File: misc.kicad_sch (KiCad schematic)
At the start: 9 parts, among them J1 BUZZER, J2 BURNER, J3 BATT, Q1 PSMN7R0, Q2 PSMN7R0

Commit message: First version for PCB
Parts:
- added J4: BAKCBONE, Connector_PinSocket_2.54mm:PinSocket_2x10_P2.54mm_Horizontal, symbol Connector_Generic:Conn_02x10_Odd_Even
- R10, R9: footprint Resistor_SMD:R_0603_1608Metric -> Resistor_SMD:R_0402_1005Metric
- R11: value 10k -> 55k
- R12: value 5k -> 55k
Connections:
- net BURNER: now also J4.13 (Pin_13), J4.14 (Pin_14)
- net BUZZER: now also J4.15 (Pin_15), J4.16 (Pin_16)
- net GND: now also J4.1 (Pin_1), J4.19 (Pin_19), J4.2 (Pin_2), J4.20 (Pin_20)
- net VOLT_SENSE: now also J4.7 (Pin_7), J4.8 (Pin_8)
- new net +3.3V: J4.17 (Pin_17), J4.18 (Pin_18)
- new net +4V: J4.3 (Pin_3), J4.4 (Pin_4)
- new net CURR_3V3: J4.11 (Pin_11), J4.12 (Pin_12)
- new net CURR_4V: J4.10 (Pin_10), J4.9 (Pin_9)
- no-connect marks 0 -> 2
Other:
- note added: "TO BACKBONE"

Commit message: Added debug things
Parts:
- added J5: DEB, Connector_PinSocket_2.54mm:PinSocket_1x06_P2.54mm_Vertical, symbol Connector_Generic:Conn_01x06
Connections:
- net +3.3V: now also J5.3 (Pin_3)
- net +4V: now also J5.2 (Pin_2)
- net BURNER: now also J5.5 (Pin_5)
- net BUZZER: now also J5.4 (Pin_4)
- net GND: now also J5.1 (Pin_1)
- net VDD: now also J5.6 (Pin_6)
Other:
- note added: "DEBUG"
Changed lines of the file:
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@@
+    (stroke (width 0) (type default) (color 0 0 0 0))
+  )
+  (wire (pts (xy 176.53 121.92) (xy 177.8 121.92))
+    (stroke (width 0) (type default) (color 0 0 0 0))
+  )
+  (polyline (pts (xy 152.4 88.9) (xy 152.4 139.7))
+    (stroke (width 0) (type default) (color 0 0 0 0))
+  )
+  (wire (pts (xy 176.53 114.3) (xy 177.8 114.3))
     (stroke (width 0) (type default) (color 0 0 0 0))
   )
@@
     (stroke (width 0) (type default) (color 0 0 0 0))
   )
+  (polyline (pts (xy 203.2 139.7) (xy 203.2 88.9))
+    (stroke (width 0) (type default) (color 0 0 0 0))
+  )
   (polyline (pts (xy 76.2 76.2) (xy 25.4 76.2))
     (stroke (width 0) (type default) (color 0 0 0 0))
@@
     (stroke (width 0) (type default) (color 0 0 0 0))
   )
+  (polyline (pts (xy 152.4 88.9) (xy 203.2 88.9))
+    (stroke (width 0) (type default) (color 0 0 0 0))
+  )
+  (wire (pts (xy 176.53 119.38) (xy 177.8 119.38))
+    (stroke (width 0) (type default) (color 0 0 0 0))
+  )
   (wire (pts (xy 55.88 44.45) (xy 54.61 44.45))
     (stroke (width 0) (type default) (color 0 0 0 0))
@@
     (stroke (width 0) (type default) (color 0 0 0 0))
   )
+  (wire (pts (xy 177.8 111.76) (xy 177.8 110.49))
+    (stroke (width 0) (type default) (color 0 0 0 0))
+  )
   (wire (pts (xy 115.57 121.92) (xy 115.57 123.19))
     (stroke (width 0) (type default) (color 0 0 0 0))
@@
     (stroke (width 0) (type default) (color 0 0 0 0))
   )
+  (wire (pts (xy 177.8 124.46) (xy 177.8 125.73))
+    (stroke (width 0) (type default) (color 0 0 0 0))
+  )
   (wire (pts (xy 151.13 184.15) (xy 151.13 185.42))
     (stroke (width 0) (type default) (color 0 0 0 0))
   )
+  (wire (pts (xy 176.53 111.76) (xy 177.8 111.76))
+    (stroke (width 0) (type default) (color 0 0 0 0))
+  )
+  (wire (pts (xy 176.53 116.84) (xy 177.8 116.84))
+    (stroke (width 0) (type default) (color 0 0 0 0))
+  )
   (wire (pts (xy 184.15 63.5) (xy 185.42 63.5))
     (stroke (width 0) (type default) (color 0 0 0 0))
@@
     (stroke (width 0) (type default) (color 0 0 0 0))
   )
+  (polyline (pts (xy 152.4 139.7) (xy 203.2 139.7))
+    (stroke (width 0) (type default) (color 0 0 0 0))
+  )
   (wire (pts (xy 151.13 176.53) (xy 151.13 177.8))
     (stroke (width 0) (type default) (color 0 0 0 0))
@@
   )
   (wire (pts (xy 55.88 124.46) (xy 55.88 127))
+    (stroke (width 0) (type default) (color 0 0 0 0))
+  )
+  (wire (pts (xy 176.53 124.46) (xy 177.8 124.46))
     (stroke (width 0) (type default) (color 0 0 0 0))
   )
@@
     (effects (font (size 2.54 2.54)) (justify left bottom))
   )
+  (text "DEBUG" (at 157.48 97.79 0)
+    (effects (font (size 2.54 2.54)) (justify left bottom))
+  )
   (text "WIRE BURNER" (at 30.48 97.79 0)
     (effects (font (size 2.54 2.54)) (justify left bottom))
@@
     )
   )
+  (global_label "3V3" (shape input) (at 177.8 119.38 0) (fields_autoplaced)
+    (effects (font (size 1.27 1.27)) (justify left))
+    (property "Intersheet References" "${INTERSHEET_REFS}" (id 0) (at 183.7207 119.4594 0)
+      (effects (font (size 1.27 1.27)) (justify left) hide)
+    )
+  )
   (global_label "BUZZER" (shape input) (at 39.37 55.88 180) (fields_autoplaced)
     (effects (font (size 1.27 1.27)) (justify right))
@@
     )
   )
+  (global_label "BUZZER" (shape input) (at 177.8 116.84 0) (fields_autoplaced)
+    (effects (font (size 1.27 1.27)) (justify left))
+    (property "Intersheet References" "${INTERSHEET_REFS}" (id 0) (at 187.6517 116.9194 0)
+      (effects (font (size 1.27 1.27)) (justify left) hide)
+    )
+  )
   (global_label "VOLT_SENSE" (shape input) (at 185.42 50.8 0) (fields_autoplaced)
     (effects (font (size 1.27 1.27)) (justify left))
@@
     )
   )
+  (global_label "BURNER" (shape input) (at 177.8 114.3 0) (fields_autoplaced)
+    (effects (font (size 1.27 1.27)) (justify left))
+    (property "Intersheet References" "${INTERSHEET_REFS}" (id 0) (at 187.8331 114.3794 0)
+      (effects (font (size 1.27 1.27)) (justify left) hide)
+    )
+  )
   (global_label "BUZZER" (shape input) (at 185.42 60.96 0) (fields_autoplaced)
     (effects (font (size 1.27 1.27)) (justify left))
@@
     (effects (font (size 1.27 1.27)) (justify left))
     (property "Intersheet References" "${INTERSHEET_REFS}" (id 0) (at 196.2393 53.2606 0)
+      (effects (font (size 1.27 1.27)) (justify left) hide)
+    )
+  )
+  (global_label "4V" (shape input) (at 177.8 121.92 0) (fields_autoplaced)
+    (effects (font (size 1.27 1.27)) (justify left))
+    (property "Intersheet References" "${INTERSHEET_REFS}" (id 0) (at 182.5112 121.9994 0)
       (effects (font (size 1.27 1.27)) (justify left) hide)
     )
@@
     (pin "1")
   )
+  (symbol (lib_id "power:VDD") (at 177.8 110.49 0) (unit 1)
+    (in_bom yes) (on_board yes) (fields_autoplaced)
+    (property "Reference" "#PWR0134" (id 0) (at 177.8 114.3 0)
+      (effects (font (size 1.27 1.27)) hide)
+    )
+    (property "Value" "VDD" (id 1) (at 177.8 105.41 0))
+    (property "Footprint" "" (id 2) (at 177.8 110.49 0)
+      (effects (font (size 1.27 1.27)) hide)
+    )
+    (property "Datasheet" "" (id 3) (at 177.8 110.49 0)
+      (effects (font (size 1.27 1.27)) hide)
+    )
+    (pin "1")
+  )
   (symbol (lib_id "power:+4V") (at 151.13 176.53 0) (unit 1)
     (in_bom yes) (on_board yes) (fields_autoplaced)
-    (property "Reference" "#PWR?" (id 0) (at 151.13 180.34 0)
+    (property "Reference" "#PWR0132" (id 0) (at 151.13 180.34 0)
       (effects (font (size 1.27 1.27)) hide)
     )
@@
     (pin "1")
   )
+  (symbol (lib_id "Connector_Generic:Conn_01x06") (at 171.45 119.38 180) (unit 1)
+    (in_bom yes) (on_board yes) (fields_autoplaced)
+    (property "Reference" "J5" (id 0) (at 171.45 105.41 0))
+    (property "Value" "DEB" (id 1) (at 171.45 107.95 0))
+    (property "Footprint" "Connector_PinSocket_2.54mm:PinSocket_1x06_P2.54mm_Vertical" (id 2) (at 171.45 119.38 0)
+      (effects (font (size 1.27 1.27)) hide)
+    )
+    (property "Datasheet" "~" (id 3) (at 171.45 119.38 0)
+      (effects (font (size 1.27 1.27)) hide)
+    )
+    (pin "1")
+    (pin "2")
+    (pin "3")
+    (pin "4")
+    (pin "5")
+    (pin "6")
+  )
   (symbol (lib_id "power:GND") (at 109.22 50.8 0) (unit 1)
     (in_bom yes) (on_board yes) (fields_autoplaced)
@@
     (pin "2")
   )
+  (symbol (lib_id "power:GND") (at 177.8 125.73 0) (unit 1)
+    (in_bom yes) (on_board yes) (fields_autoplaced)
+    (property "Reference" "#PWR0135" (id 0) (at 177.8 132.08 0)
+      (effects (font (size 1.27 1.27)) hide)
+    )
+    (property "Value" "GND" (id 1) (at 177.8 130.81 0))
+    (property "Footprint" "" (id 2) (at 177.8 125.73 0)
+      (effects (font (size 1.27 1.27)) hide)
+    )
+    (property "Datasheet" "" (id 3) (at 177.8 125.73 0)
+      (effects (font (size 1.27 1.27)) hide)
+    )
+    (pin "1")
+  )
   (symbol (lib_id "power:VDD") (at 55.88 40.64 0) (unit 1)
     (in_bom yes) (on_board yes) (fields_autoplaced)
@@
   (symbol (lib_id "power:+3.3V") (at 161.29 176.53 0) (unit 1)
     (in_bom yes) (on_board yes) (fields_autoplaced)
-    (property "Reference" "#PWR?" (id 0) (at 161.29 180.34 0)
+    (property "Reference" "#PWR0133" (id 0) (at 161.29 180.34 0)
       (effects (font (size 1.27 1.27)) hide)
     )
@@
   (symbol (lib_id "power:GND") (at 151.13 185.42 0) (unit 1)
     (in_bom yes) (on_board yes) (fields_autoplaced)
-    (property "Reference" "#PWR?" (id 0) (at 151.13 191.77 0)
-      (effects (font (size 1.27 1.27)) hide)
-    )
+    (property "Reference" "#PWR0131" (id 0) (at 151.13 191.77 0)
+      (effects (font (size 1.27 1.27)) hide)
+    )

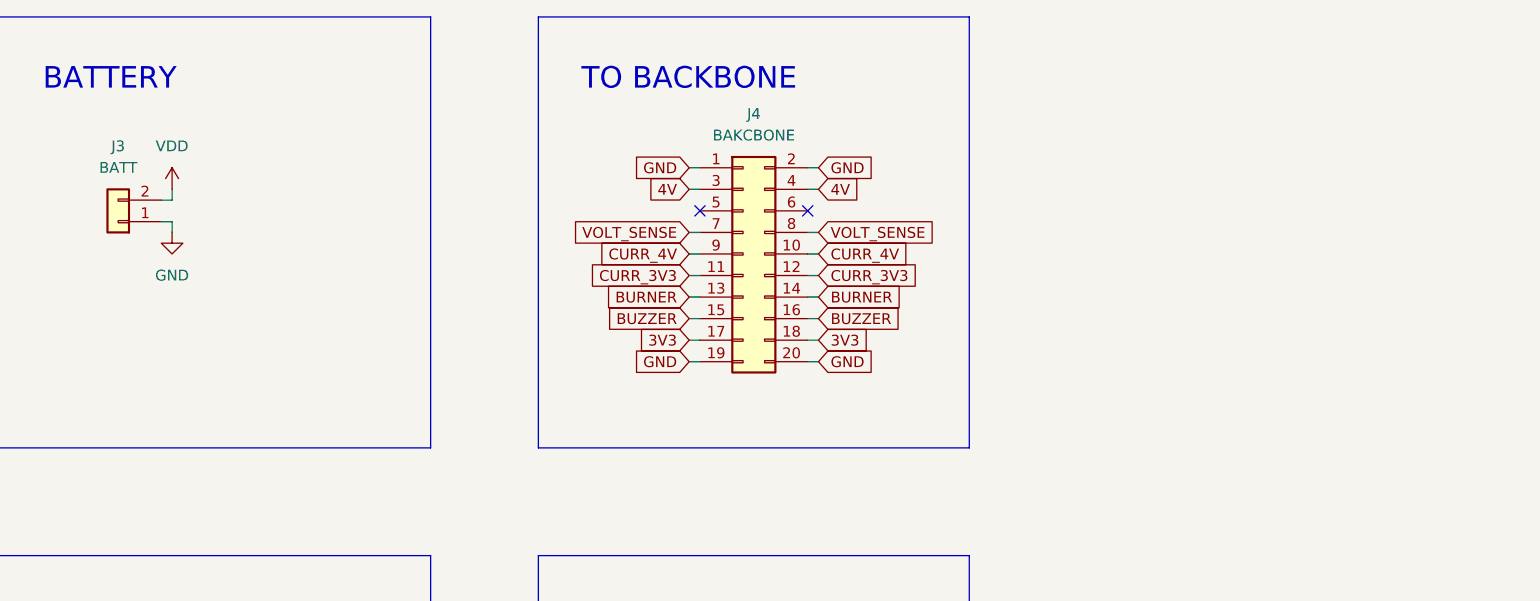
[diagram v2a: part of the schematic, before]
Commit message: Reverse polarity protection
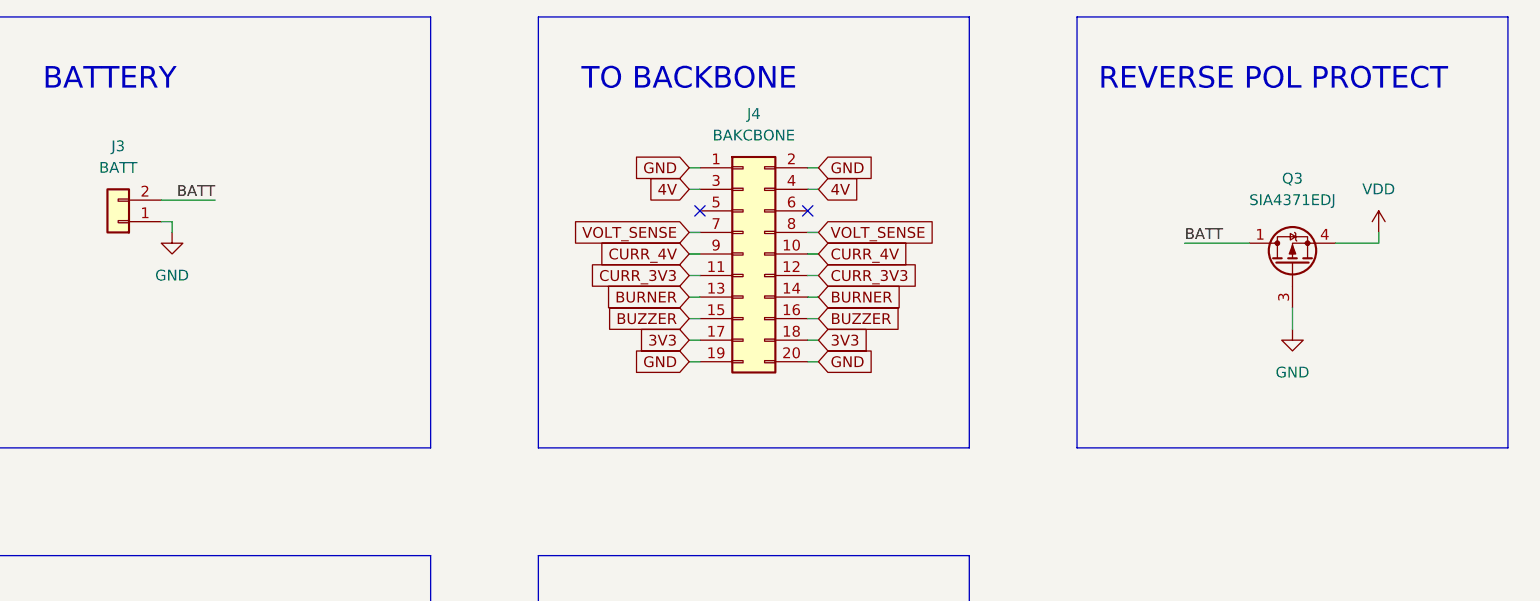
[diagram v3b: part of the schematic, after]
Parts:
- added Q3: SIA4371EDJ, Package_TO_SOT_SMD:Vishay_PowerPAK_SC70-6L_Single, symbol Transistor_FET:SiA453EDJ
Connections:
- net GND: now also Q3.3 (G)
- net VDD: now also Q3.4 (S); no longer J3.2 (Pin_2)
- new net BATT: J3.2 (Pin_2), Q3.1 (D)
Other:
- note added: "REVERSE POL PROTECT"
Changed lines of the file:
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@@
   (no_connect (at 171.45 48.26))
   (no_connect (at 184.15 48.26))
+  (polyline (pts (xy 215.9 76.2) (xy 266.7 76.2))
+    (stroke (width 0) (type default) (color 0 0 0 0))
+  )
   (polyline (pts (xy 139.7 76.2) (xy 139.7 25.4))
     (stroke (width 0) (type default) (color 0 0 0 0))
@@
     (stroke (width 0) (type default) (color 0 0 0 0))
   )
+  (wire (pts (xy 251.46 52.07) (xy 246.38 52.07))
+    (stroke (width 0) (type default) (color 0 0 0 0))
+  )
   (wire (pts (xy 170.18 63.5) (xy 171.45 63.5))
     (stroke (width 0) (type default) (color 0 0 0 0))
@@
     (stroke (width 0) (type default) (color 0 0 0 0))
   )
-  (wire (pts (xy 109.22 45.72) (xy 109.22 46.99))
-    (stroke (width 0) (type default) (color 0 0 0 0))
-  )
   (polyline (pts (xy 76.2 25.4) (xy 76.2 76.2))
     (stroke (width 0) (type default) (color 0 0 0 0))
@@
     (stroke (width 0) (type default) (color 0 0 0 0))
   )
+  (wire (pts (xy 251.46 50.8) (xy 251.46 52.07))
+    (stroke (width 0) (type default) (color 0 0 0 0))
+  )
   (wire (pts (xy 177.8 111.76) (xy 177.8 110.49))
     (stroke (width 0) (type default) (color 0 0 0 0))
@@
     (stroke (width 0) (type default) (color 0 0 0 0))
   )
-  (wire (pts (xy 109.22 46.99) (xy 107.95 46.99))
+  (wire (pts (xy 107.95 46.99) (xy 114.3 46.99))
     (stroke (width 0) (type default) (color 0 0 0 0))
   )
@@
     (stroke (width 0) (type default) (color 0 0 0 0))
   )
+  (polyline (pts (xy 266.7 76.2) (xy 266.7 25.4))
+    (stroke (width 0) (type default) (color 0 0 0 0))
+  )
   (wire (pts (xy 170.18 50.8) (xy 171.45 50.8))
     (stroke (width 0) (type default) (color 0 0 0 0))
@@
     (stroke (width 0) (type default) (color 0 0 0 0))
   )
+  (polyline (pts (xy 215.9 25.4) (xy 215.9 76.2))
+    (stroke (width 0) (type default) (color 0 0 0 0))
+  )
   (wire (pts (xy 44.45 119.38) (xy 48.26 119.38))
     (stroke (width 0) (type default) (color 0 0 0 0))
@@
     (stroke (width 0) (type default) (color 0 0 0 0))
   )
+  (wire (pts (xy 241.3 59.69) (xy 241.3 62.23))
+    (stroke (width 0) (type default) (color 0 0 0 0))
+  )
   (wire (pts (xy 44.45 63.5) (xy 55.88 63.5))
     (stroke (width 0) (type default) (color 0 0 0 0))
@@
     (stroke (width 0) (type default) (color 0 0 0 0))
   )
+  (polyline (pts (xy 215.9 25.4) (xy 266.7 25.4))
+    (stroke (width 0) (type default) (color 0 0 0 0))
+  )
   (wire (pts (xy 39.37 55.88) (xy 44.45 55.88))
+    (stroke (width 0) (type default) (color 0 0 0 0))
+  )
+  (wire (pts (xy 228.6 52.07) (xy 236.22 52.07))
     (stroke (width 0) (type default) (color 0 0 0 0))
   )
@@
     (effects (font (size 2.54 2.54)) (justify left bottom))
   )
+  (text "REVERSE POL PROTECT" (at 218.44 34.29 0)
+    (effects (font (size 2.54 2.54)) (justify left bottom))
+  )
   (text "DEBUG" (at 157.48 97.79 0)
     (effects (font (size 2.54 2.54)) (justify left bottom))
@@
     (effects (font (size 2.54 2.54)) (justify left bottom))
   )
+  (label "BATT" (at 114.3 46.99 180)
+    (effects (font (size 1.27 1.27)) (justify right bottom))
+  )
+  (label "BATT" (at 228.6 52.07 0)
+    (effects (font (size 1.27 1.27)) (justify left bottom))
+  )
   (global_label "GND" (shape input) (at 170.18 66.04 180) (fields_autoplaced)
     (effects (font (size 1.27 1.27)) (justify right))
@@
       (effects (font (size 1.27 1.27)) (justify left) hide)
     )
+  )
+  (symbol (lib_id "power:VDD") (at 251.46 50.8 0) (unit 1)
+    (in_bom yes) (on_board yes) (fields_autoplaced)
+    (property "Reference" "#PWR0126" (id 0) (at 251.46 54.61 0)
+      (effects (font (size 1.27 1.27)) hide)
+    )
+    (property "Value" "VDD" (id 1) (at 251.46 45.72 0))
+    (property "Footprint" "" (id 2) (at 251.46 50.8 0)
+      (effects (font (size 1.27 1.27)) hide)
+    )
+    (property "Datasheet" "" (id 3) (at 251.46 50.8 0)
+      (effects (font (size 1.27 1.27)) hide)
+    )
+    (pin "1")
   )
   (symbol (lib_id "power:VDD") (at 115.57 107.95 0) (unit 1)
@@
     (pin "9")
   )
-  (symbol (lib_id "power:VDD") (at 109.22 45.72 0) (unit 1)
-    (in_bom yes) (on_board yes) (fields_autoplaced)
-    (property "Reference" "#PWR0126" (id 0) (at 109.22 49.53 0)
-      (effects (font (size 1.27 1.27)) hide)
-    )
-    (property "Value" "VDD" (id 1) (at 109.22 40.64 0))
-    (property "Footprint" "" (id 2) (at 109.22 45.72 0)
-      (effects (font (size 1.27 1.27)) hide)
-    )
-    (property "Datasheet" "" (id 3) (at 109.22 45.72 0)
-      (effects (font (size 1.27 1.27)) hide)
-    )
-    (pin "1")
-  )
   (symbol (lib_id "power:VDD") (at 177.8 110.49 0) (unit 1)
     (in_bom yes) (on_board yes) (fields_autoplaced)
@@
     (pin "6")
   )
+  (symbol (lib_id "Transistor_FET:SiA453EDJ") (at 241.3 54.61 90) (unit 1)
+    (in_bom yes) (on_board yes) (fields_autoplaced)
+    (property "Reference" "Q3" (id 0) (at 241.3 44.45 90))
+    (property "Value" "SIA4371EDJ" (id 1) (at 241.3 46.99 90))
+    (property "Footprint" "Package_TO_SOT_SMD:Vishay_PowerPAK_SC70-6L_Single" (id 2) (at 243.205 49.53 0)
+      (effects (font (size 1.27 1.27) italic) (justify left) hide)
+    )
+    (property "Datasheet" "http://www.vishay.com/docs/62864/sia453edj.pdf" (id 3) (at 241.3 54.61 90)
+      (effects (font (size 1.27 1.27)) (justify left) hide)
+    )
+    (pin "1")
+    (pin "3")
+    (pin "4")
+  )
   (symbol (lib_id "power:GND") (at 109.22 50.8 0) (unit 1)
     (in_bom yes) (on_board yes) (fields_autoplaced)
@@
       (effects (font (size 1.27 1.27)) hide)
     )
+    (pin "1")
+  )
+  (symbol (lib_id "power:GND") (at 241.3 62.23 0) (unit 1)
+    (in_bom yes) (on_board yes) (fields_autoplaced)
+    (property "Reference" "#PWR?" (id 0) (at 241.3 68.58 0)
+      (effects (font (size 1.27 1.27)) hide)
+    )
+    (property "Value" "GND" (id 1) (at 241.3 67.31 0))
+    (property "Footprint" "" (id 2) (at 241.3 62.23 0)
+      (effects (font (size 1.27 1.27)) hide)
+    )
+    (property "Datasheet" "" (id 3) (at 241.3 62.23 0)
+      (effects (font (size 1.27 1.27)) hide)
+    )

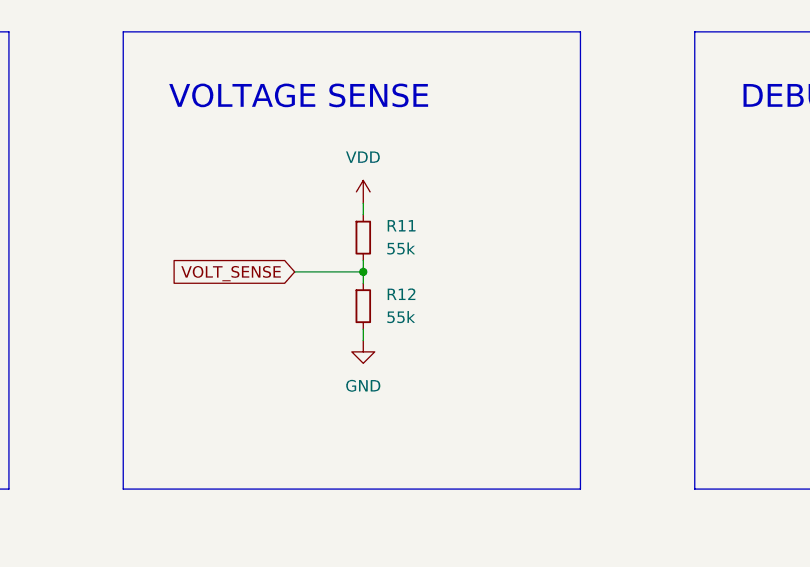
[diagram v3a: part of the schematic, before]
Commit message: Changed ressistor values
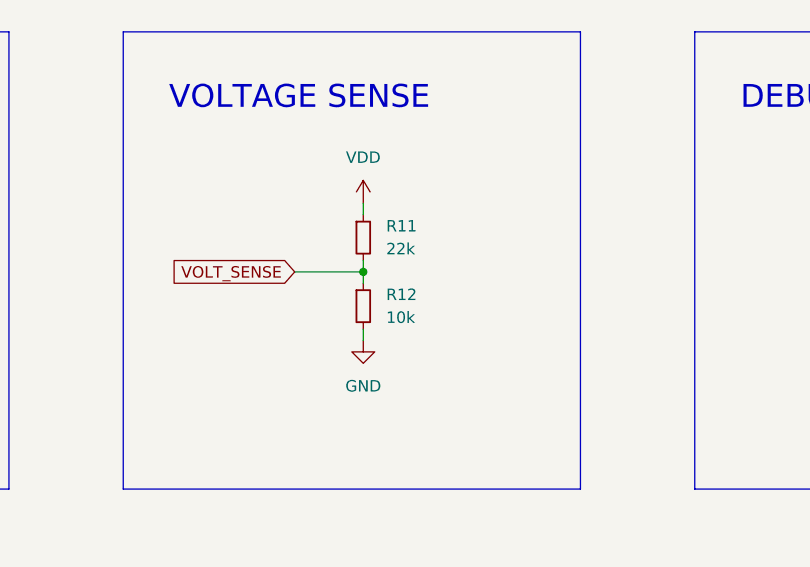
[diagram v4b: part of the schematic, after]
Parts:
- R11: value 55k -> 22k
- R12: value 55k -> 10k
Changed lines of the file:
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@@
       (effects (font (size 1.27 1.27)) (justify left))
     )
-    (property "Value" "55k" (id 1) (at 118.11 113.0299 0)
+    (property "Value" "22k" (id 1) (at 118.11 113.0299 0)
       (effects (font (size 1.27 1.27)) (justify left))
     )
@@
       (effects (font (size 1.27 1.27)) (justify left))
     )
-    (property "Value" "55k" (id 1) (at 118.11 120.6499 0)
+    (property "Value" "10k" (id 1) (at 118.11 120.6499 0)
       (effects (font (size 1.27 1.27)) (justify left))
     )
